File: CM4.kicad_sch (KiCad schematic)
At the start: 4 parts

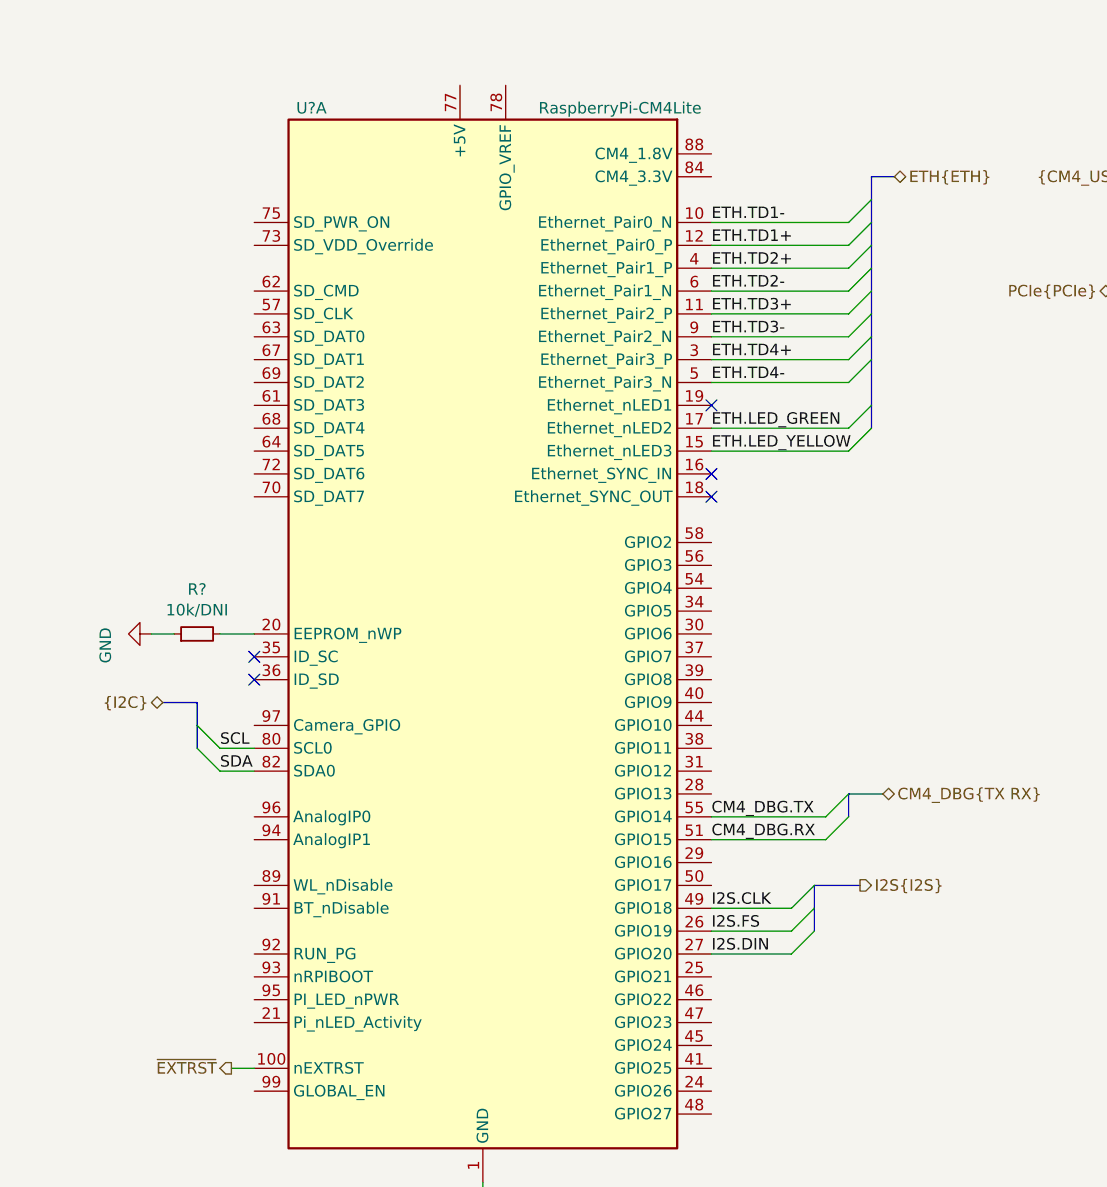
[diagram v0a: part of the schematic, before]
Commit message: Changes     -Added sdcard sheet and SD bus     -changed main i2c bus     -added 1.8V and 3.3V connection to CM4     -removed clk32 from led driver     -fixed PCM interface Data pin
Signed-off-by: Dominik Sliwa <dominik@sliwa.io>
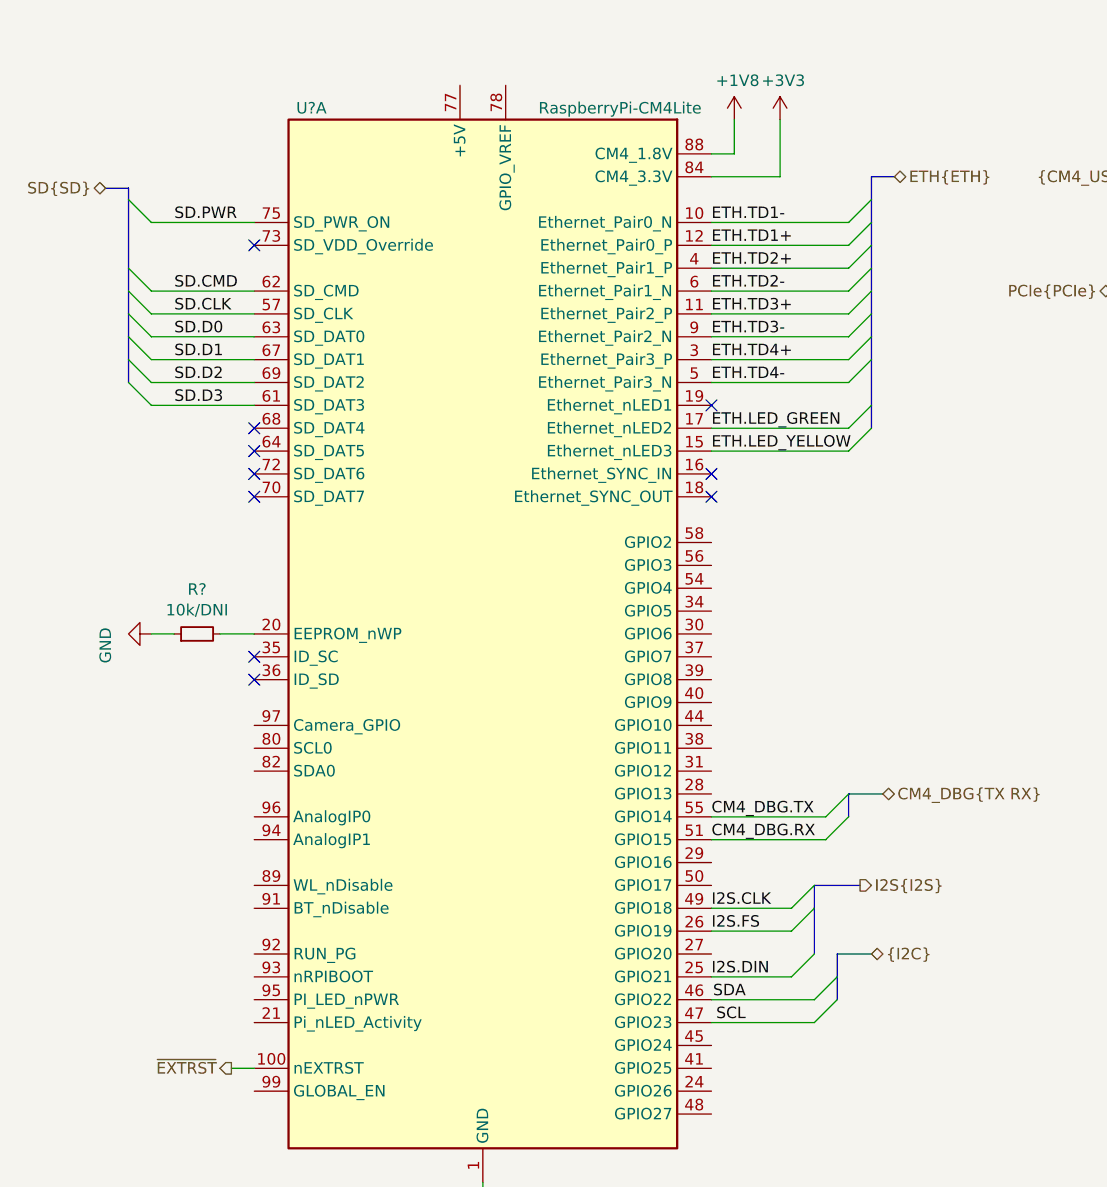
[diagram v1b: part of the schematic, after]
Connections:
- net I2S.DIN: now also U?.25 (GPIO21); no longer U?.27 (GPIO20)
- net SCL: now also U?.47 (GPIO23); no longer U?.80 (SCL0)
- net SDA: now also U?.46 (GPIO22); no longer U?.82 (SDA0)
- net SD.CLK: now reaches U?.57 (SD_CLK)
- net SD.D3: now reaches U?.61 (SD_DAT3)
- net SD.CMD: now reaches U?.62 (SD_CMD)
- net SD.D0: now reaches U?.63 (SD_DAT0)
- net SD.D1: now reaches U?.67 (SD_DAT1)
- net SD.D2: now reaches U?.69 (SD_DAT2)
- net SD.PWR: now reaches U?.75 (SD_PWR_ON)
- net +3V3: now reaches U?.84 (CM4_3.3V), U?.86 (CM4_3.3V)
- net +1V8: now reaches U?.88 (CM4_1.8V), U?.90 (CM4_1.8V)
- no-connect marks 51 -> 56

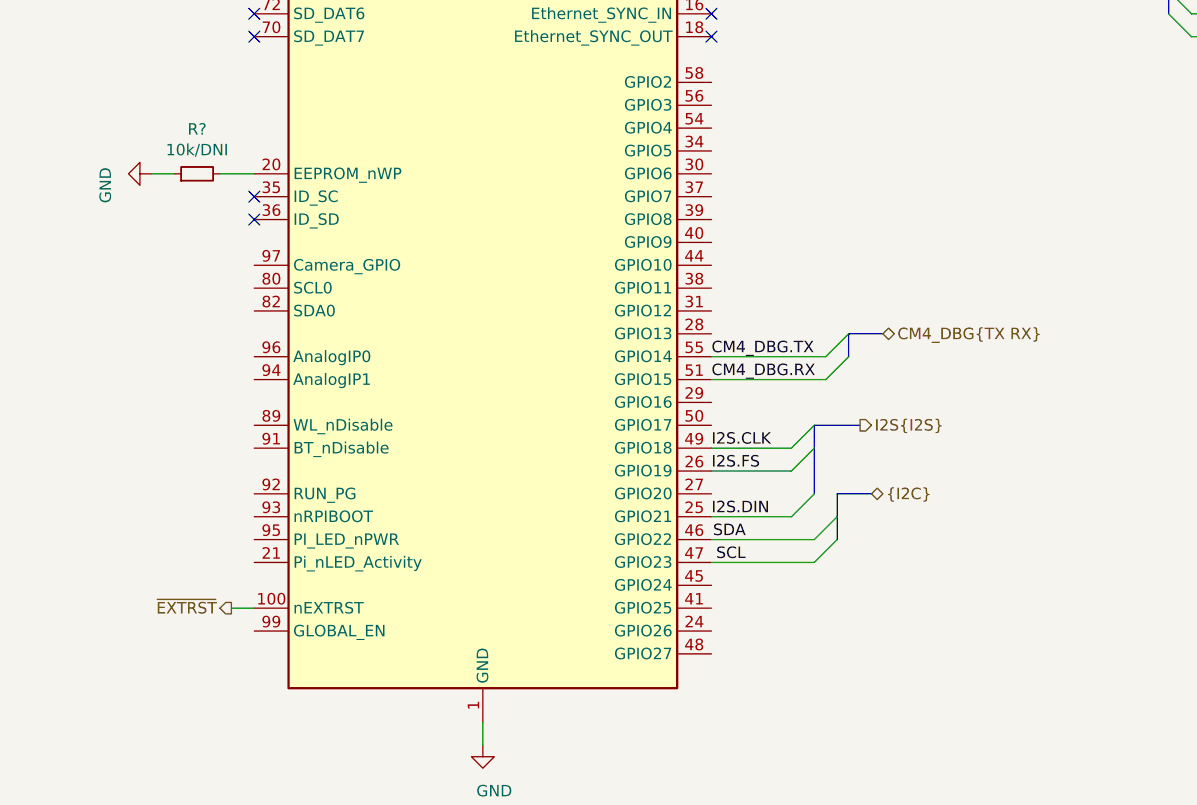
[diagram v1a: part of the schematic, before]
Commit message: Add UART for Zigbee and wire up control signals
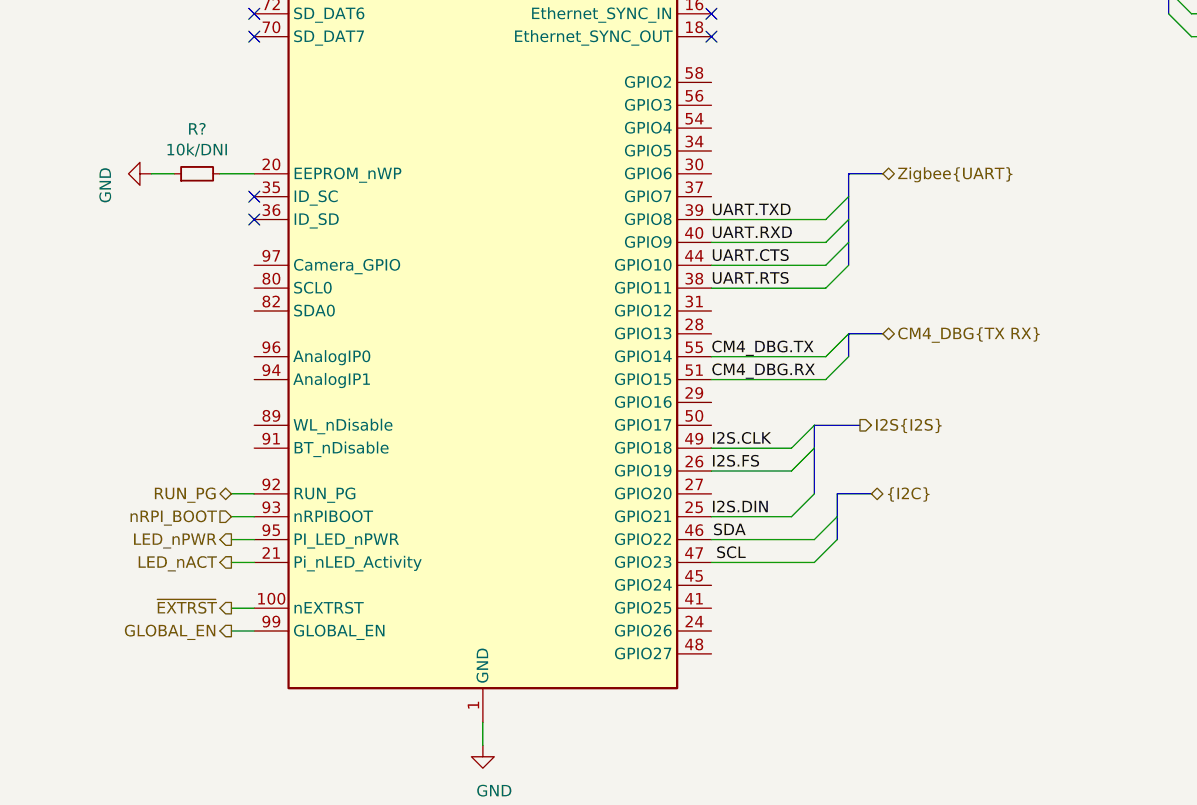
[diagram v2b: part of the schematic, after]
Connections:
- net LED_nACT: now reaches U?.21 (Pi_nLED_Activity)
- net UART.RTS: now reaches U?.38 (GPIO11)
- net UART.TXD: now reaches U?.39 (GPIO8)
- net UART.RXD: now reaches U?.40 (GPIO9)
- net UART.CTS: now reaches U?.44 (GPIO10)
- net RUN_PG: now reaches U?.92 (RUN_PG)
- net nRPI_BOOT: now reaches U?.93 (nRPIBOOT)
- net LED_nPWR: now reaches U?.95 (PI_LED_nPWR)
- net GLOBAL_EN: now reaches U?.99 (GLOBAL_EN)
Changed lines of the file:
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@@
 (kicad_sch (version 20201015) (generator eeschema)
   (paper "A4")
+  (bus_alias "HDMI" (members "D0+" "D0-" "D1+" "D1-" "D2+" "D2-" "CLK+" "CLK-" "CEC" "HPD" "SDA" "SCL"))
+  (bus_alias "PCIe" (members "~RST" "~CLKREQ" "CLK+" "CLK-" "TX+" "TX-" "RX+" "RX-"))
   (bus_alias "SD" (members "D[0..3]" "CMD" "CLK" "PWR"))
-  (bus_alias "PCIe" (members "~RST" "~CLKREQ" "CLK+" "CLK-" "TX+" "TX-" "RX+" "RX-"))
-  (bus_alias "HDMI" (members "D0+" "D0-" "D1+" "D1-" "D2+" "D2-" "CLK+" "CLK-" "CEC" "HPD" "SDA" "SCL"))
   (junction (at 260.35 82.55) (diameter 1.016) (color 0 0 0 0))
   (junction (at 262.89 82.55) (diameter 1.016) (color 0 0 0 0))
@@
   (junction (at 267.97 82.55) (diameter 1.016) (color 0 0 0 0))
   (junction (at 270.51 82.55) (diameter 1.016) (color 0 0 0 0))
-  (no_connect (at 210.82 55.88))
-  (no_connect (at 210.82 129.54))
-  (no_connect (at 160.02 35.56))
-  (no_connect (at 210.82 132.08))
-  (no_connect (at 210.82 40.64))
-  (no_connect (at 210.82 43.18))
-  (no_connect (at 160.02 116.84))
-  (no_connect (at 160.02 114.3))
-  (no_connect (at 210.82 48.26))
-  (no_connect (at 210.82 53.34))
-  (no_connect (at 210.82 137.16))
-  (no_connect (at 210.82 60.96))
-  (no_connect (at 210.82 111.76))
-  (no_connect (at 160.02 119.38))
-  (no_connect (at 210.82 114.3))
-  (no_connect (at 210.82 35.56))
   (no_connect (at 38.1 45.72))
-  (no_connect (at 210.82 109.22))
-  (no_connect (at 160.02 104.14))
-  (no_connect (at 210.82 104.14))
-  (no_connect (at 160.02 109.22))
-  (no_connect (at 210.82 38.1))
   (no_connect (at 38.1 66.04))
   (no_connect (at 38.1 68.58))
   (no_connect (at 38.1 71.12))
   (no_connect (at 38.1 73.66))
-  (no_connect (at 210.82 101.6))
   (no_connect (at 38.1 91.44))
-  (no_connect (at 160.02 81.28))
-  (no_connect (at 210.82 121.92))
-  (no_connect (at 160.02 83.82))
-  (no_connect (at 210.82 119.38))
-  (no_connect (at 160.02 86.36))
   (no_connect (at 38.1 93.98))
-  (no_connect (at 210.82 127))
-  (no_connect (at 160.02 91.44))
-  (no_connect (at 88.9 73.66))
-  (no_connect (at 255.27 67.31))
-  (no_connect (at 160.02 121.92))
-  (no_connect (at 210.82 106.68))
-  (no_connect (at 160.02 106.68))
-  (no_connect (at 160.02 88.9))
-  (no_connect (at 210.82 139.7))
-  (no_connect (at 210.82 45.72))
-  (no_connect (at 210.82 58.42))
-  (no_connect (at 210.82 124.46))
-  (no_connect (at 210.82 142.24))
-  (no_connect (at 210.82 63.5))
-  (no_connect (at 160.02 93.98))
-  (no_connect (at 210.82 134.62))
-  (no_connect (at 210.82 50.8))
-  (no_connect (at 160.02 99.06))
   (no_connect (at 88.9 63.5))
   (no_connect (at 88.9 71.12))
+  (no_connect (at 88.9 73.66))
+  (no_connect (at 160.02 35.56))
+  (no_connect (at 160.02 81.28))
+  (no_connect (at 160.02 83.82))
+  (no_connect (at 160.02 86.36))
+  (no_connect (at 160.02 88.9))
+  (no_connect (at 160.02 91.44))
+  (no_connect (at 160.02 93.98))
+  (no_connect (at 160.02 99.06))
+  (no_connect (at 160.02 101.6))
+  (no_connect (at 160.02 104.14))
+  (no_connect (at 160.02 106.68))
+  (no_connect (at 160.02 109.22))
   (no_connect (at 160.02 111.76))
-  (no_connect (at 160.02 101.6))
+  (no_connect (at 160.02 114.3))
+  (no_connect (at 160.02 116.84))
+  (no_connect (at 160.02 119.38))
+  (no_connect (at 160.02 121.92))
+  (no_connect (at 210.82 35.56))
+  (no_connect (at 210.82 38.1))
+  (no_connect (at 210.82 40.64))
+  (no_connect (at 210.82 43.18))
+  (no_connect (at 210.82 45.72))
+  (no_connect (at 210.82 48.26))
+  (no_connect (at 210.82 50.8))
+  (no_connect (at 210.82 53.34))
+  (no_connect (at 210.82 55.88))
+  (no_connect (at 210.82 58.42))
+  (no_connect (at 210.82 60.96))
+  (no_connect (at 210.82 63.5))
+  (no_connect (at 210.82 101.6))
+  (no_connect (at 210.82 104.14))
+  (no_connect (at 210.82 106.68))
+  (no_connect (at 210.82 109.22))
+  (no_connect (at 210.82 111.76))
+  (no_connect (at 210.82 114.3))
+  (no_connect (at 210.82 119.38))
+  (no_connect (at 210.82 121.92))
+  (no_connect (at 210.82 124.46))
+  (no_connect (at 210.82 127))
+  (no_connect (at 210.82 129.54))
+  (no_connect (at 210.82 132.08))
+  (no_connect (at 210.82 134.62))
+  (no_connect (at 210.82 137.16))
+  (no_connect (at 210.82 139.7))
+  (no_connect (at 210.82 142.24))
+  (no_connect (at 255.27 67.31))
   (bus_entry (at 24.13 40.64) (size 2.54 2.54)
     (stroke (width 0.1524) (type solid) (color 0 0 0 0))
@@
     (stroke (width 0.1524) (type solid) (color 0 0 0 0))
   )
+  (bus_entry (at 104.14 91.44) (size -2.54 2.54)
+    (stroke (width 0.1524) (type solid) (color 0 0 0 0))
+  )
+  (bus_entry (at 104.14 93.98) (size -2.54 2.54)
+    (stroke (width 0.1524) (type solid) (color 0 0 0 0))
+  )
+  (bus_entry (at 104.14 96.52) (size -2.54 2.54)
+    (stroke (width 0.1524) (type solid) (color 0 0 0 0))
+  )
+  (bus_entry (at 104.14 99.06) (size -2.54 2.54)
+    (stroke (width 0.1524) (type solid) (color 0 0 0 0))
+  )
   (bus_entry (at 104.14 106.68) (size -2.54 2.54)
     (stroke (width 0.1524) (type solid) (color 0 0 0 0))
@@
     (stroke (width 0) (type solid) (color 0 0 0 0))
   )
+  (wire (pts (xy 35.56 124.46) (xy 38.1 124.46))
+    (stroke (width 0) (type solid) (color 0 0 0 0))
+  )
+  (wire (pts (xy 35.56 127) (xy 38.1 127))
+    (stroke (width 0) (type solid) (color 0 0 0 0))
+  )
+  (wire (pts (xy 35.56 129.54) (xy 38.1 129.54))
+    (stroke (width 0) (type solid) (color 0 0 0 0))
+  )
+  (wire (pts (xy 35.56 132.08) (xy 38.1 132.08))
+    (stroke (width 0) (type solid) (color 0 0 0 0))
+  )
   (wire (pts (xy 35.56 137.16) (xy 38.1 137.16))
     (stroke (width 0) (type solid) (color 0 0 0 0))
   )
+  (wire (pts (xy 35.56 139.7) (xy 38.1 139.7))
+    (stroke (width 0) (type solid) (color 0 0 0 0))
+  )
   (wire (pts (xy 63.5 149.86) (xy 63.5 152.4))
     (stroke (width 0) (type solid) (color 0 0 0 0))
@@
     (stroke (width 0) (type solid) (color 0 0 0 0))
   )
+  (wire (pts (xy 88.9 93.98) (xy 101.6 93.98))
+    (stroke (width 0) (type solid) (color 0 0 0 0))
+  )
+  (wire (pts (xy 88.9 96.52) (xy 101.6 96.52))
+    (stroke (width 0) (type solid) (color 0 0 0 0))
+  )
+  (wire (pts (xy 88.9 99.06) (xy 101.6 99.06))
+    (stroke (width 0) (type solid) (color 0 0 0 0))
+  )
+  (wire (pts (xy 88.9 101.6) (xy 101.6 101.6))
+    (stroke (width 0) (type solid) (color 0 0 0 0))
+  )
   (wire (pts (xy 88.9 109.22) (xy 101.6 109.22))
     (stroke (width 0) (type solid) (color 0 0 0 0))
@@
     (stroke (width 0) (type solid) (color 0 0 0 0))
   )
+  (bus (pts (xy 104.14 88.9) (xy 104.14 91.44))
+    (stroke (width 0) (type solid) (color 0 0 0 0))
+  )
+  (bus (pts (xy 104.14 91.44) (xy 104.14 93.98))
+    (stroke (width 0) (type solid) (color 0 0 0 0))
+  )
+  (bus (pts (xy 104.14 93.98) (xy 104.14 96.52))
+    (stroke (width 0) (type solid) (color 0 0 0 0))
+  )
+  (bus (pts (xy 104.14 96.52) (xy 104.14 99.06))
+    (stroke (width 0) (type solid) (color 0 0 0 0))
+  )
   (bus (pts (xy 104.14 106.68) (xy 107.95 106.68))
     (stroke (width 0) (type solid) (color 0 0 0 0))
@@
     (stroke (width 0) (type solid) (color 0 0 0 0))
   )
+  (bus (pts (xy 107.95 88.9) (xy 104.14 88.9))
+    (stroke (width 0) (type solid) (color 0 0 0 0))
+  )
   (bus (pts (xy 133.35 50.8) (xy 139.7 50.8))
     (stroke (width 0) (type solid) (color 0 0 0 0))
@@
   )
   (label "ETH.LED_YELLOW" (at 88.9 68.58 0)
+    (effects (font (size 1.27 1.27)) (justify left bottom))
+  )
+  (label "UART.TXD" (at 88.9 93.98 0)
+    (effects (font (size 1.27 1.27)) (justify left bottom))
+  )
+  (label "UART.RXD" (at 88.9 96.52 0)
+    (effects (font (size 1.27 1.27)) (justify left bottom))
+  )
+  (label "UART.CTS" (at 88.9 99.06 0)
+    (effects (font (size 1.27 1.27)) (justify left bottom))
+  )
+  (label "UART.RTS" (at 88.9 101.6 0)
     (effects (font (size 1.27 1.27)) (justify left bottom))
   )
@@
     (effects (font (size 1.27 1.27)) (justify right))
   )
+  (hierarchical_label "RUN_PG" (shape bidirectional) (at 35.56 124.46 180)
+    (effects (font (size 1.27 1.27)) (justify right))
+  )
+  (hierarchical_label "nRPI_BOOT" (shape input) (at 35.56 127 180)
+    (effects (font (size 1.27 1.27)) (justify right))
+  )
+  (hierarchical_label "LED_nPWR" (shape output) (at 35.56 129.54 180)
+    (effects (font (size 1.27 1.27)) (justify right))
+  )
+  (hierarchical_label "LED_nACT" (shape output) (at 35.56 132.08 180)
+    (effects (font (size 1.27 1.27)) (justify right))
+  )
   (hierarchical_label "~EXTRST" (shape output) (at 35.56 137.16 180)
     (effects (font (size 1.27 1.27)) (justify right))
   )
+  (hierarchical_label "GLOBAL_EN" (shape output) (at 35.56 139.7 180)
+    (effects (font (size 1.27 1.27)) (justify right))
+  )
   (hierarchical_label "I2S{I2S}" (shape output) (at 105.41 116.84 0)
     (effects (font (size 1.27 1.27)) (justify left))
@@
     (effects (font (size 1.27 1.27)) (justify left))
   )
+  (hierarchical_label "Zigbee{UART}" (shape bidirectional) (at 107.95 88.9 0)
+    (effects (font (size 1.27 1.27)) (justify left))
+  )
